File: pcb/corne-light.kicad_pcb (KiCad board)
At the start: 2 copper layers, 275.5 x 105.6 mm, 172 parts, among them J1 MJ-4PP-9, J2 OLED, J5 Breakaway_Tabs, J6 MJ-4PP-9, J7 OLED, Q1 Q_NPN_BEC, Q2 Q_NPN_BEC, SW1 Rotary_Encoder_Switch, SW40 Rotary_Encoder_Switch, U1 ProMicro, U2 ProMicro

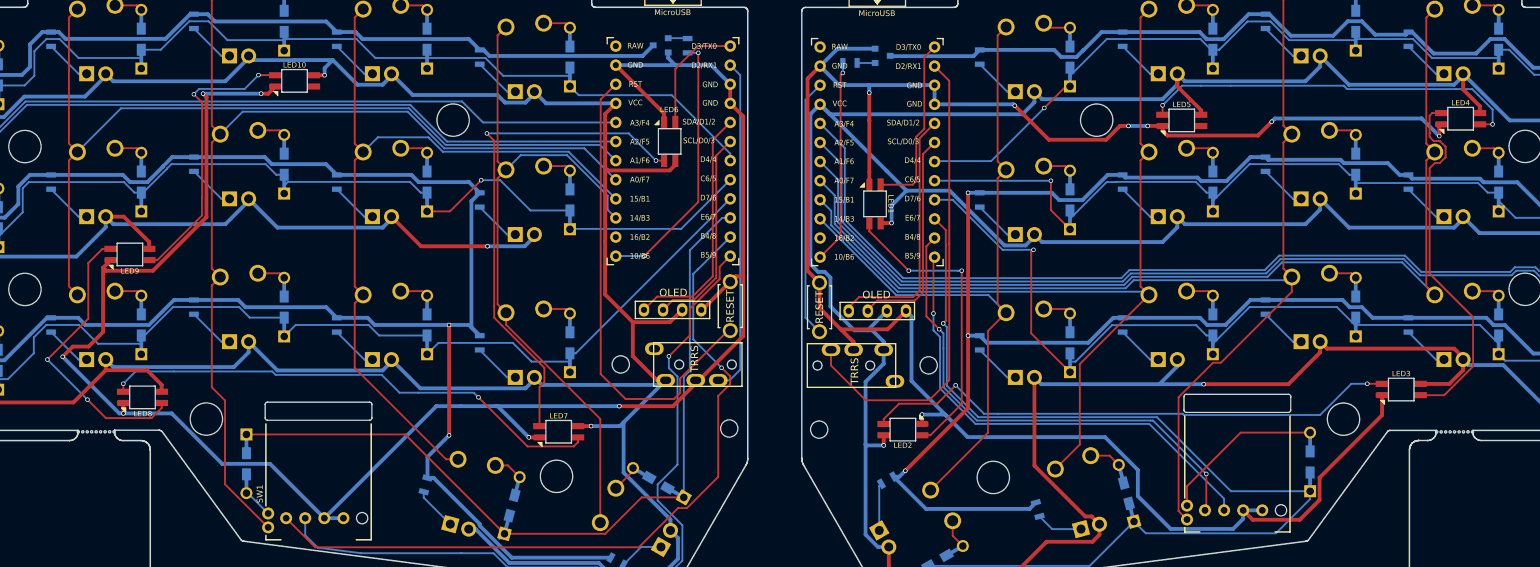
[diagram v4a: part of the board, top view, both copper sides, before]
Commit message: Remove RGB and add a new image
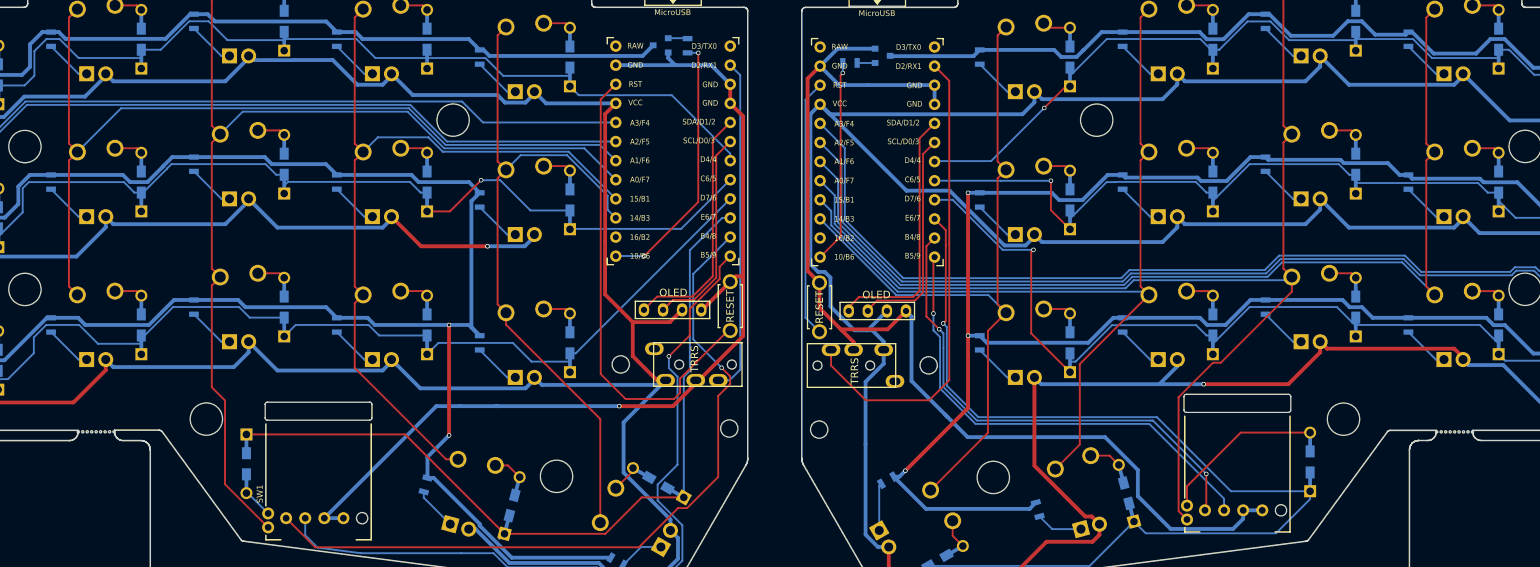
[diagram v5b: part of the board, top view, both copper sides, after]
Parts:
- removed LED1, LED10, LED2, LED3, LED4, LED5, LED6, LED7, LED8, LED9: YS-SK6812MINI-E, Keebio-Parts:SK6812-MINI-E
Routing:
- net GND: track 251.5 -> 128.7 mm, vias 6 -> 1
- net GNDA: track 267.4 -> 146.3 mm, vias 7 -> 0
- net Net-(LED2-Pad2): track 72.1 -> 0.00 mm, vias 2 -> 0
- net Net-(LED6-Pad2): track 67.4 -> 0.00 mm, vias 2 -> 0
- net Net-(LED7-Pad2): track 67.2 -> 0.00 mm, vias 2 -> 0
- net Net-(LED4-Pad2): track 51.2 -> 0.00 mm, vias 2 -> 0
- net Net-(LED3-Pad2): track 48.7 -> 0.00 mm
- net Net-(LED1-Pad2): track 40.3 -> 0.00 mm, vias 2 -> 0
- net Net-(LED8-Pad2): track 38.5 -> 0.00 mm, vias 2 -> 0
- net Net-(LED10-Pad4): track 38.0 -> 0.00 mm, vias 2 -> 0
- net VCC: track 528.7 -> 490.9 mm, vias 4 -> 2
- net VDD: track 569.0 -> 537.9 mm, vias 4 -> 2
- net DIN_r: track 23.8 -> 0.00 mm
- net DIN: track 15.7 -> 0.00 mm

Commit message: Fix mosfet and add add silkscreen stuff
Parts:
- added G***: LOGO, silks:hap2, F.Cu at (118.4, 47.2)
- added G***: LOGO, silks:popop, F.Cu at (55.4, 41.7)
- added G***: LOGO, silks:dn_f, F.Cu at (221.7, 61.5)
- added G***: LOGO, silks:stare1, F.Cu at (19.9, 54.2)
- added G***: LOGO, silks:peek, F.Cu at (76.2, 98.3)
- added G***: LOGO, silks:hehe, F.Cu at (128.2, 107.6)
- added G***: LOGO, silks:ahhhh, F.Cu at (53.2, 87.5)
- added G***: LOGO, silks:dn2, F.Cu at (169.8, 61.5)
- added R43: 470, Keebio-Parts:R_0805, B.Cu at (139.1, 40.5)
- added R44: 10k, Keebio-Parts:R_0805, B.Cu at (139.2, 42.9)
- Q1, Q2: value Q_NPN_BEC -> 2N7002E
- R21: value 1k -> 470
- R22: value 1k -> 10k
- moved R22 24.0 mm to (162.8, 41.9), turned to 0 degrees
- moved Q1 2.59 mm to (167.4, 43.4)
- moved R21 2.44 mm to (162.9, 44.4)
- moved Q2 0.82 mm to (134.4, 41.9)
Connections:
- R22 pad 1: Net-(Q2-Pad1) -> Net-(Q1-Pad1)
- R22 pad 2: Net-(R22-Pad2) -> GNDA
- U1 pad 13: Net-(R22-Pad2) -> Net-(R43-Pad2)
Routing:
- net Net-(R43-Pad2): track 0.00 -> 41.4 mm, vias 0 -> 1
- net Net-(R22-Pad2): track 35.2 -> 0.00 mm, vias 2 -> 0
- net Net-(Q1-Pad1): track 2.40 -> 5.81 mm
- net GND: track 128.7 -> 131.6 mm
- net Net-(Q2-Pad1): track 2.60 -> 5.32 mm
- net PWM_r: track 429.0 -> 426.4 mm
- net Net-(R21-Pad2): track 27.1 -> 29.3 mm
- net GNDA: track 146.3 -> 148.5 mm
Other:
- board text added: "WAFFLE"

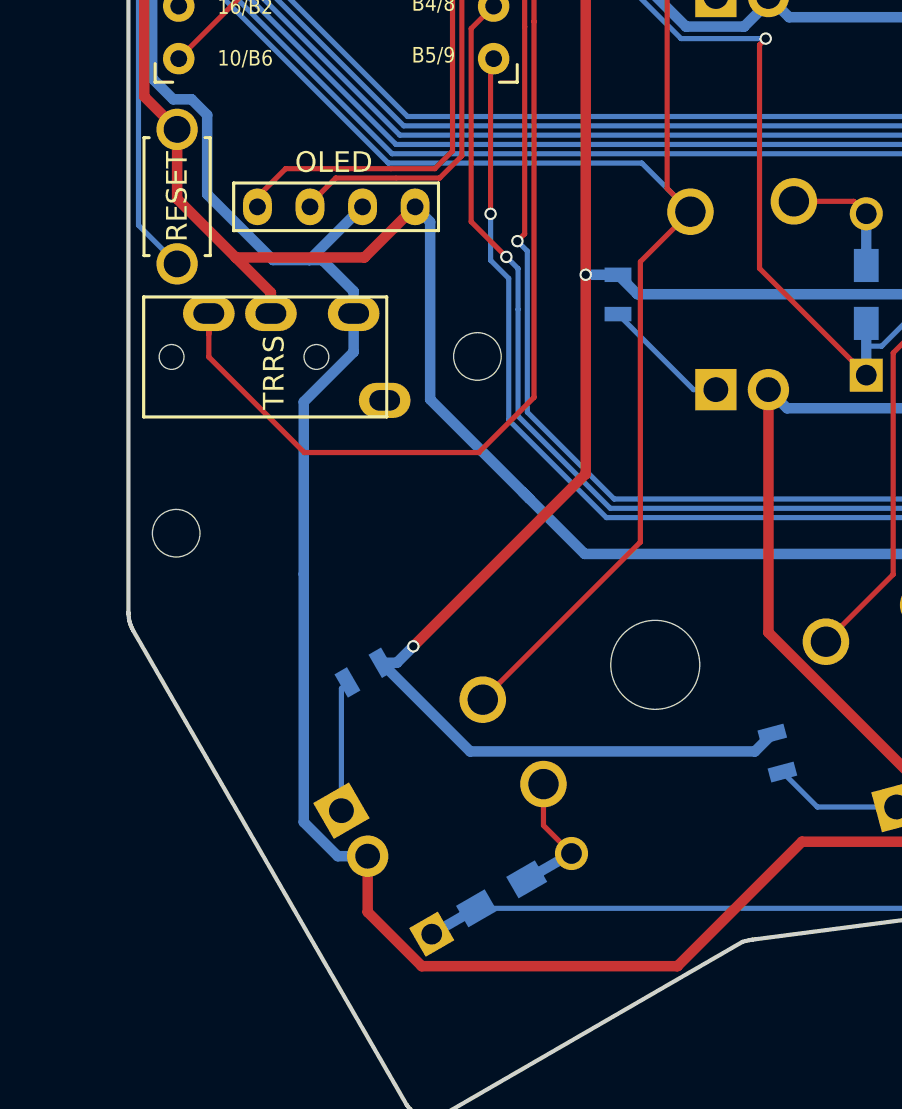
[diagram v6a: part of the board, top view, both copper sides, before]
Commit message: Add trackball support
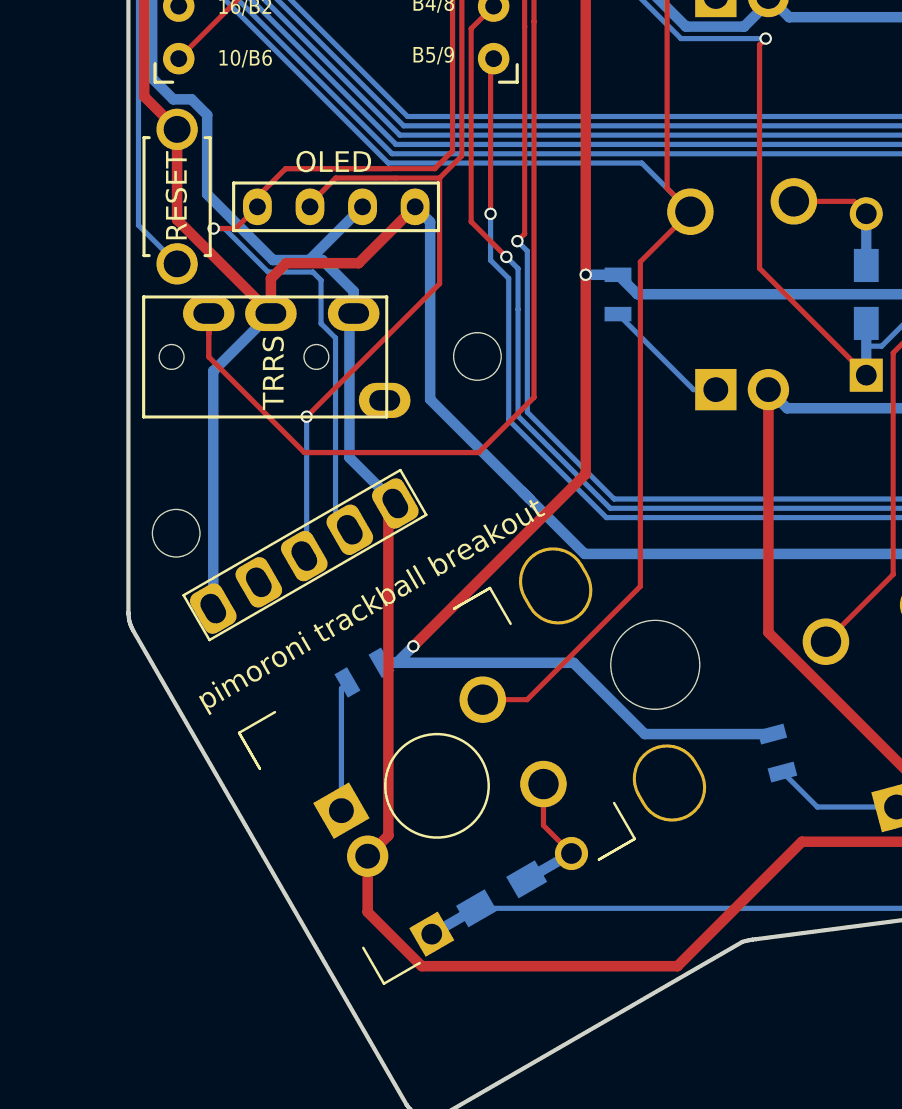
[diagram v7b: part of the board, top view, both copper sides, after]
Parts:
- added J3: Conn_01x05, other_parts:pimoroni_left_side_mount, B.Cu at (168.9, 105.3)
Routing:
- net SDA_r: track 34.0 -> 55.4 mm, vias 0 -> 1
- net SCL_r: track 29.1 -> 50.1 mm, vias 0 -> 1
- net GNDA: track 148.5 -> 164.3 mm
- net VDD: track 537.9 -> 536.3 mm
- net col5_r: track 97.5 -> 98.8 mm
- net PWM_r: track 426.4 -> 425.7 mm
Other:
- board text added: "https://github.com/ItsWaffIe/waffle_corne.git"
- board text added: "https://github.com/foostan/crkbd.git"

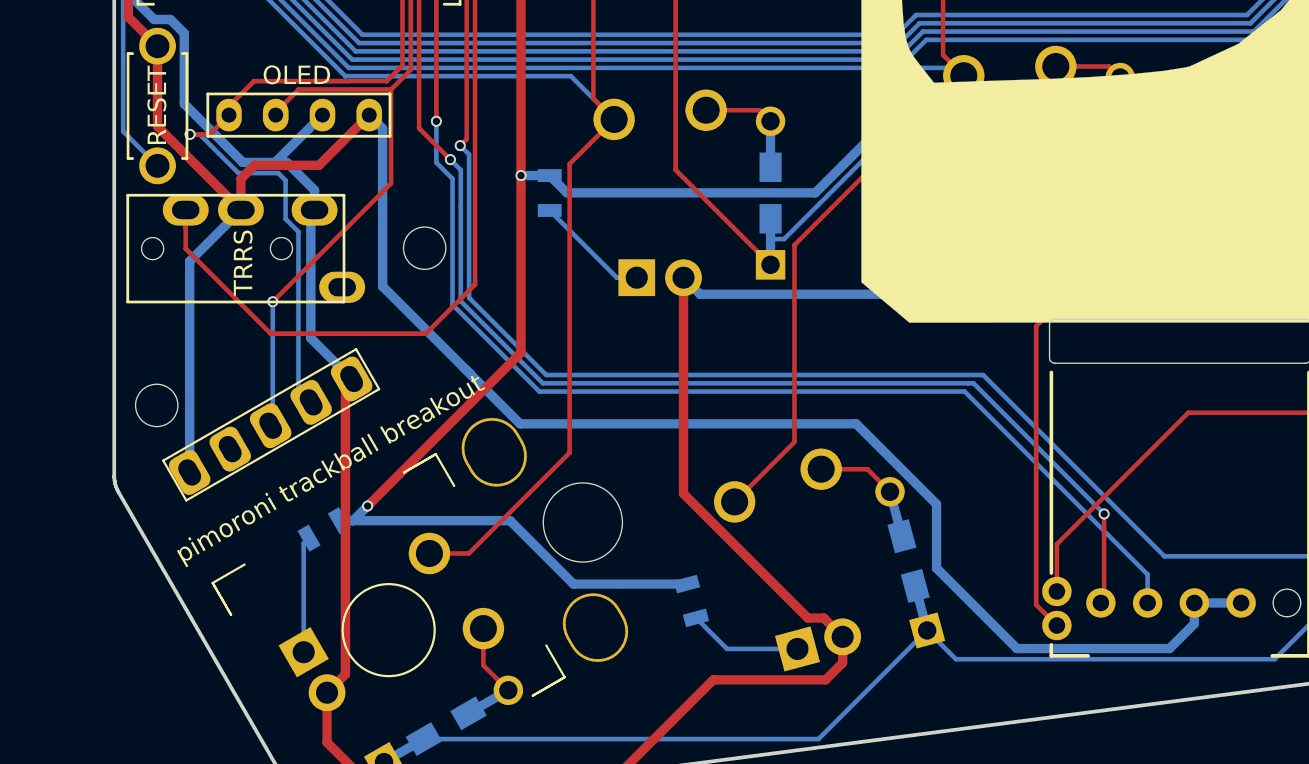
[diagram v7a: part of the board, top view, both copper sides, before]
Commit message: Remove references from silkscreen
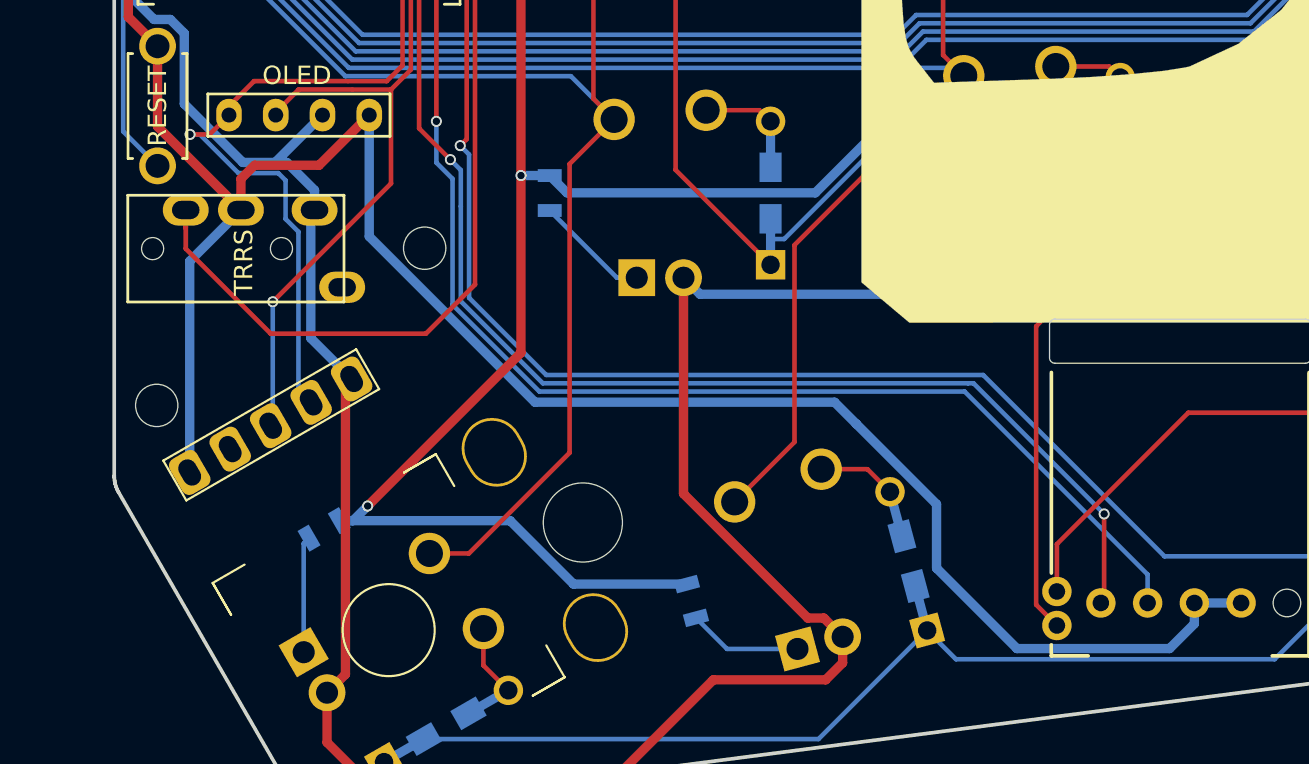
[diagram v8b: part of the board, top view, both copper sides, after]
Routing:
- net GNDA: track 164.3 -> 162.7 mm
